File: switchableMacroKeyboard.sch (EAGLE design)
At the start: 33 parts

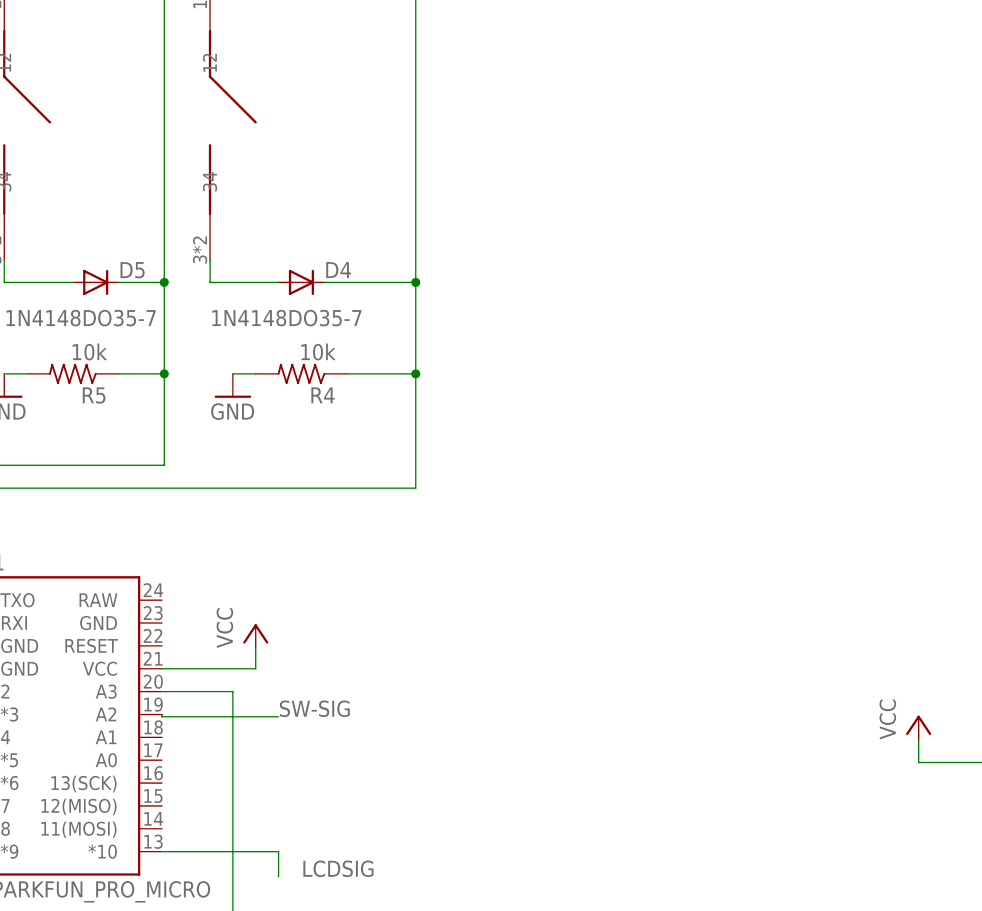
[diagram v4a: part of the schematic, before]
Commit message: Added an enable option to disable all output when broken for debugging purposes. Mitered all of the traces with a 40 mil miter. Changed the corners from filets to chamfers.
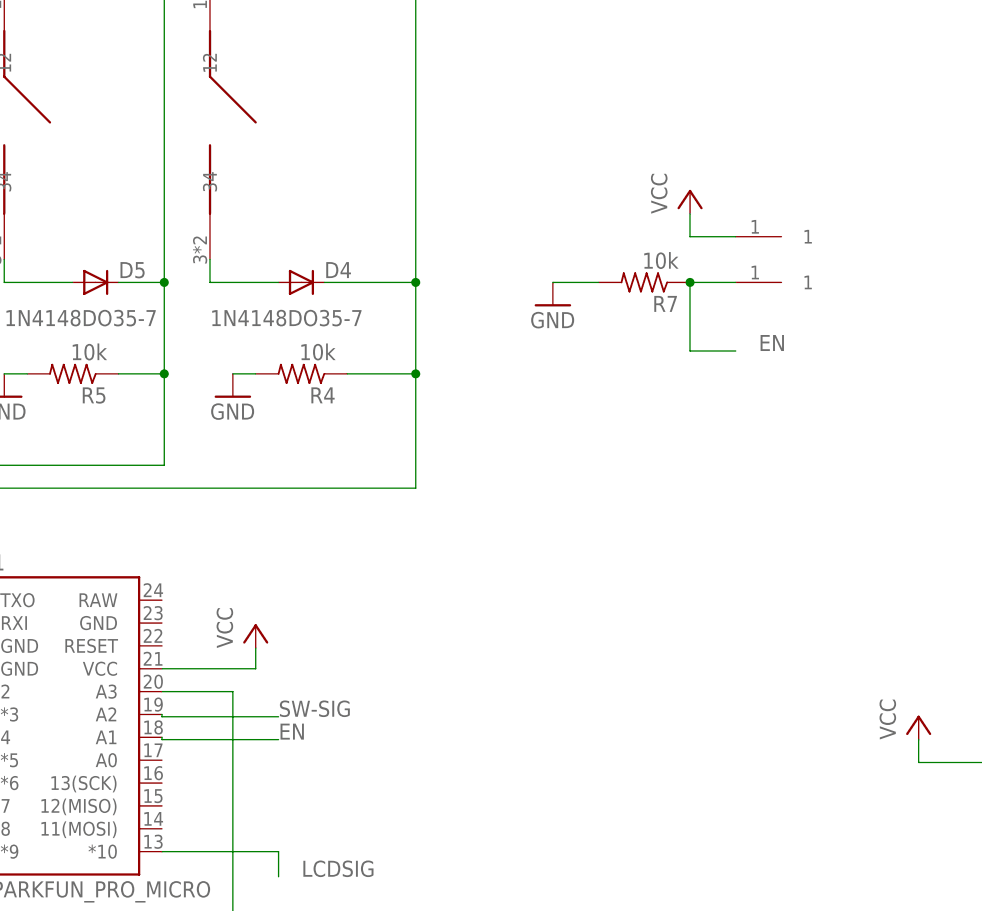
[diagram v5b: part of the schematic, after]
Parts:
- added R7: 10k, rcl:R-US_0207/10
- added U$1, U$2: TESTPOINT, ARNEConnectors:TESTPOINT
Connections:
- new net EN: B1.A1, R7.1, U$2.1
- net GND: now also R7.2
- net VCC: now also U$1.1
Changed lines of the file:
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@@
 <part name="GND6" library="supply1" library_urn="urn:adsk.eagle:library:371" deviceset="GND" device=""/>
 <part name="GND7" library="supply1" library_urn="urn:adsk.eagle:library:371" deviceset="GND" device=""/>
+<part name="U$1" library="ARNEConnectors" deviceset="TESTPOINT" device=""/>
+<part name="U$2" library="ARNEConnectors" deviceset="TESTPOINT" device=""/>
+<part name="R7" library="rcl" library_urn="urn:adsk.eagle:library:334" deviceset="R-US_" device="0207/10" package3d_urn="urn:adsk.eagle:package:23491/2" value="10k"/>
+<part name="GND8" library="supply1" library_urn="urn:adsk.eagle:library:371" deviceset="GND" device=""/>
+<part name="P+5" library="supply1" library_urn="urn:adsk.eagle:library:371" deviceset="VCC" device=""/>
 </parts>
 <sheets>
@@
 <instance part="GND7" gate="1" x="2.54" y="10.16" smashed="yes">
 <attribute name="VALUE" x="0" y="7.62" size="1.778" layer="96"/>
+</instance>
+<instance part="U$1" gate="G$1" x="106.68" y="27.94" smashed="yes"/>
+<instance part="U$2" gate="G$1" x="106.68" y="22.86" smashed="yes"/>
+<instance part="R7" gate="G$1" x="96.52" y="22.86" smashed="yes" rot="R180">
+<attribute name="NAME" x="100.33" y="21.3614" size="1.778" layer="95" rot="R180"/>
+<attribute name="VALUE" x="100.33" y="26.162" size="1.778" layer="96" rot="R180"/>
+</instance>
+<instance part="GND8" gate="1" x="86.36" y="20.32" smashed="yes">
+<attribute name="VALUE" x="83.82" y="17.78" size="1.778" layer="96"/>
+</instance>
+<instance part="P+5" gate="VCC" x="101.6" y="33.02" smashed="yes">
+<attribute name="VALUE" x="99.06" y="30.48" size="1.778" layer="96" rot="R90"/>
 </instance>
 </instances>
@@
 <wire x1="127" y1="-30.48" x2="127" y2="-27.94" width="0.1524" layer="91"/>
 </segment>
+<segment>
+<pinref part="P+5" gate="VCC" pin="VCC"/>
+<pinref part="U$1" gate="G$1" pin="1"/>
+<wire x1="101.6" y1="30.48" x2="101.6" y2="27.94" width="0.1524" layer="91"/>
+<wire x1="101.6" y1="27.94" x2="106.68" y2="27.94" width="0.1524" layer="91"/>
+</segment>
 </net>
 <net name="N$9" class="0">
@@
 <pinref part="GND5" gate="1" pin="GND"/>
 <wire x1="53.34" y1="12.7" x2="50.8" y2="12.7" width="0.1524" layer="91"/>
+</segment>
+<segment>
+<pinref part="R7" gate="G$1" pin="2"/>
+<pinref part="GND8" gate="1" pin="GND"/>
+<wire x1="91.44" y1="22.86" x2="86.36" y2="22.86" width="0.1524" layer="91"/>
 </segment>
 </net>
@@
 </segment>
 </net>
+<net name="EN" class="0">
+<segment>
+<pinref part="B1" gate="G$1" pin="A1"/>
+<wire x1="42.926" y1="-27.686" x2="42.926" y2="-27.94" width="0.1524" layer="91"/>
+<wire x1="42.926" y1="-27.94" x2="55.88" y2="-27.94" width="0.1524" layer="91"/>
+<label x="55.88" y="-27.94" size="1.778" layer="95"/>
+</segment>
+<segment>
+<pinref part="U$2" gate="G$1" pin="1"/>
+<pinref part="R7" gate="G$1" pin="1"/>
+<wire x1="101.6" y1="22.86" x2="106.68" y2="22.86" width="0.1524" layer="91"/>
+<wire x1="101.6" y1="22.86" x2="101.6" y2="15.24" width="0.1524" layer="91"/>
+<junction x="101.6" y="22.86"/>
+<wire x1="101.6" y1="15.24" x2="106.68" y2="15.24" width="0.1524" layer="91"/>
+<label x="109.22" y="15.24" size="1.778" layer="95"/>
+</segment>
+</net>

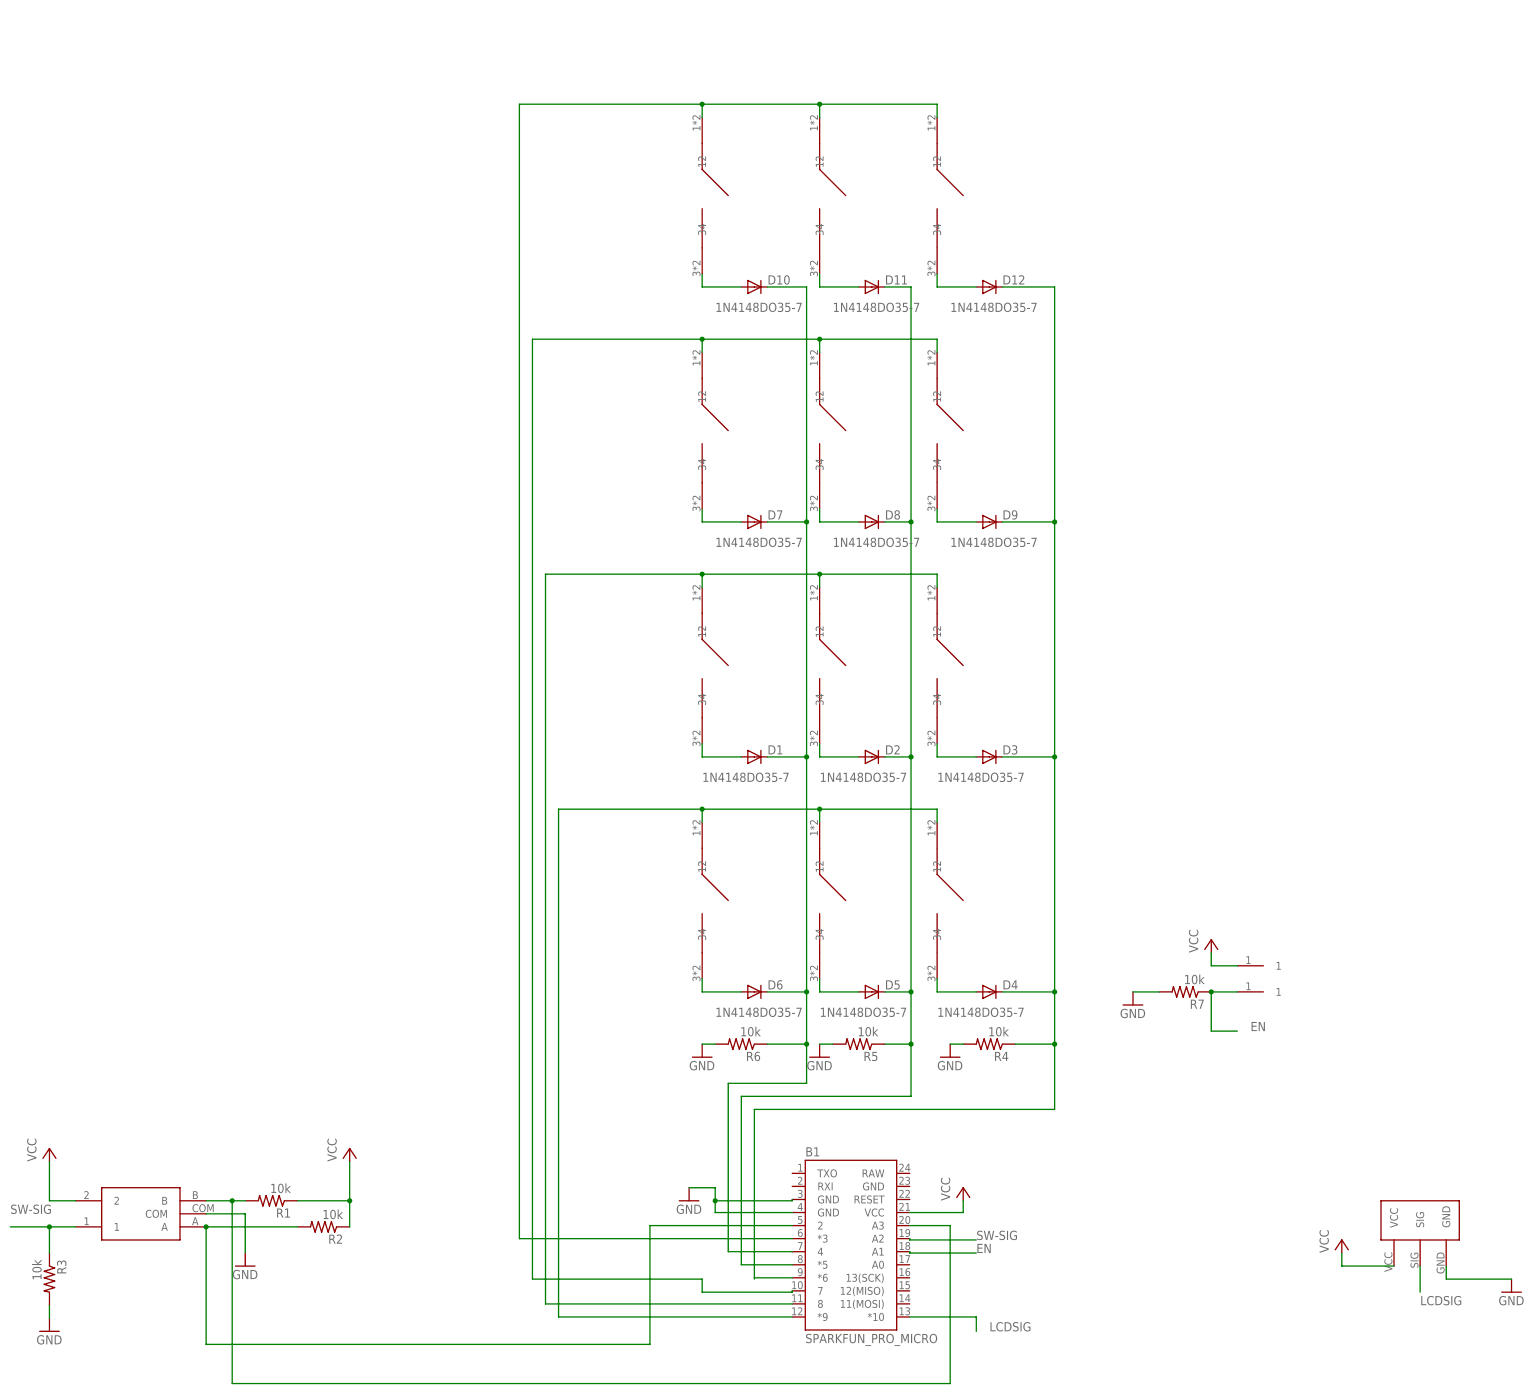
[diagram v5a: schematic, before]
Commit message: Added I2C header for LCD panel. Rearranged pinouts to open up I2C pins on the Pro Micro. To do: add labels to I2C bus and reroute board.
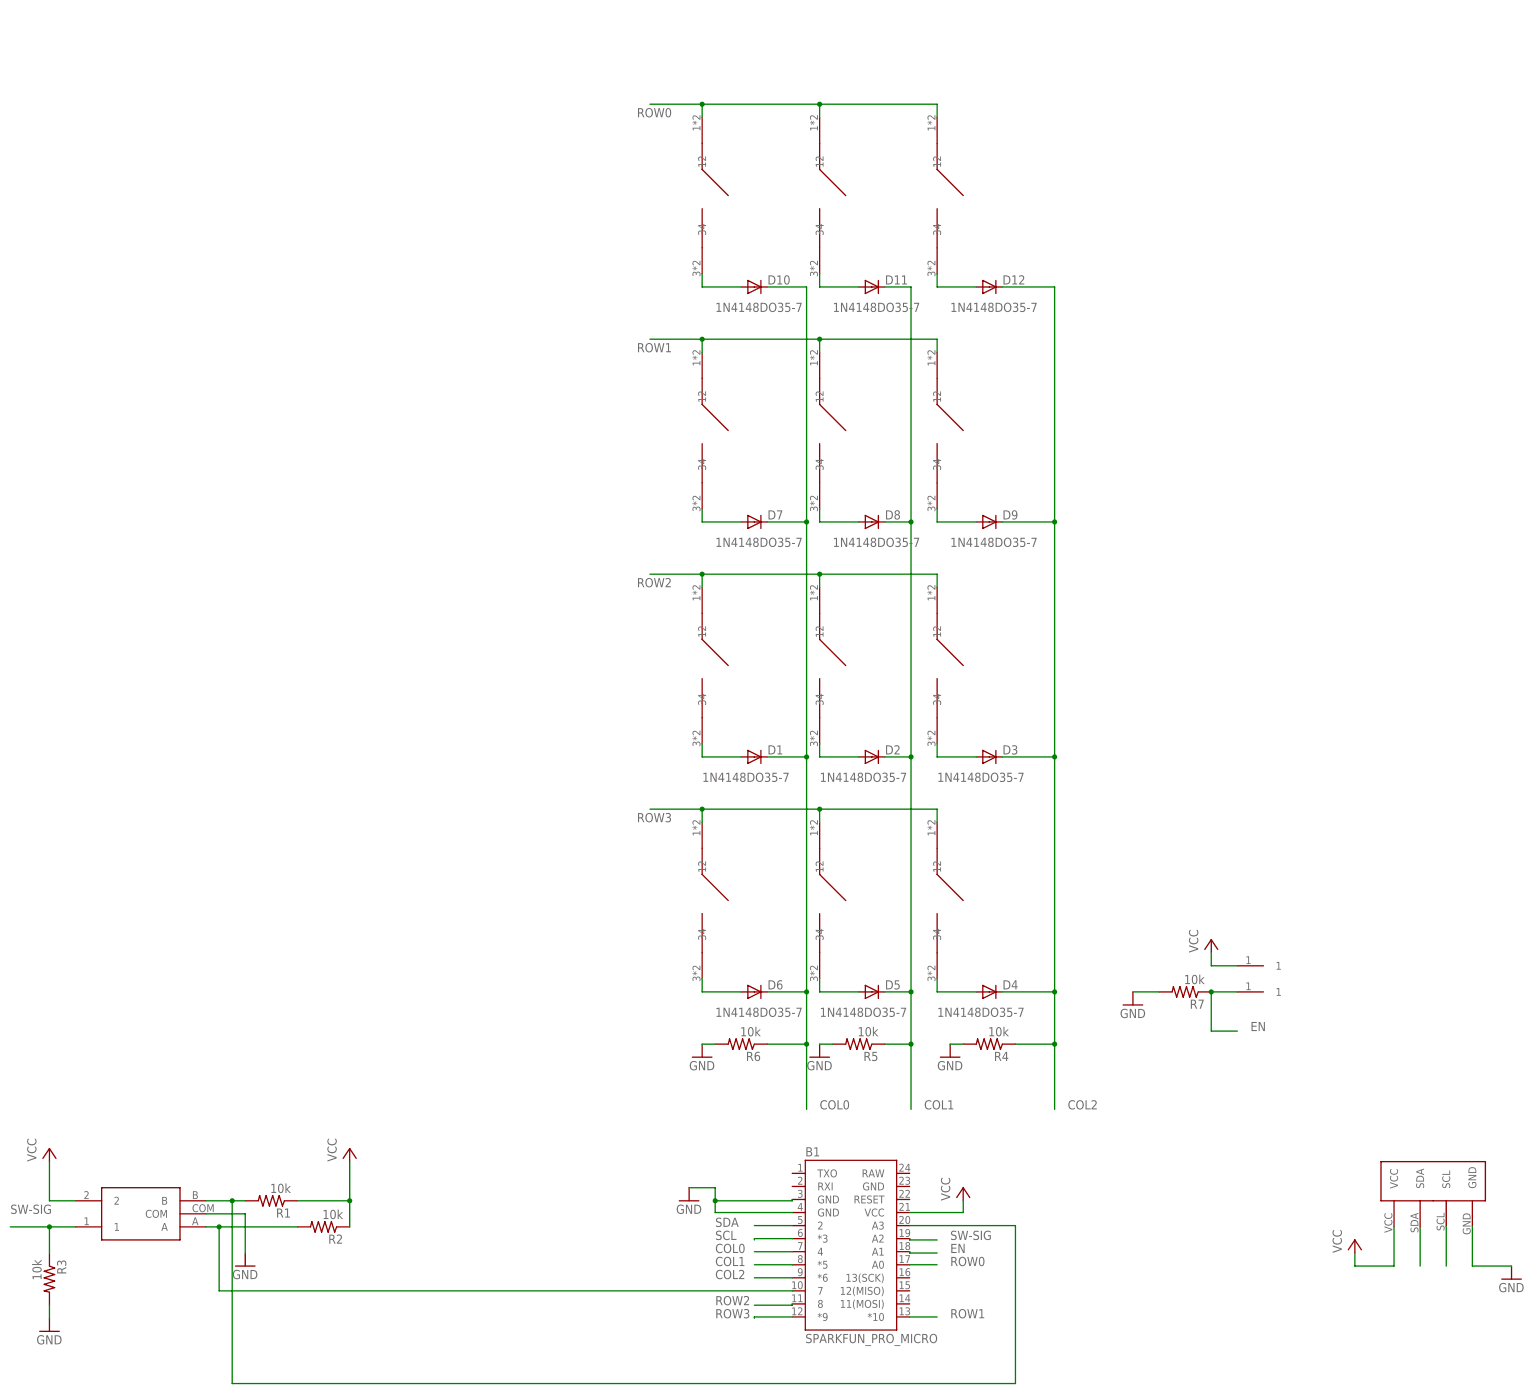
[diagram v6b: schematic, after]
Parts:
- removed U$14: 100MIL3PINSIGNAL, switchableMacroKeyboard:100MIL3PINSIGNAL
- added U$3: I2C-100MIL, ARNEConnectors:I2C-100MIL
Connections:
- net N$10 renamed ROW2
- net N$2 renamed ROW3
- net N$22 renamed COL1
- net N$28 renamed COL0
- net N$30 renamed COL2
- removed net LCDSIG: B1.*10, U$14.SIG
- removed net N$12: B1.2, R2.2, U$13.A
- removed net N$17: 10.12, 11.12, 12.12, B1.7
- removed net N$24: 00.12, 01.12, 02.12, B1.*3
- new net N$1: B1.7, R2.2, U$13.A
- new net ROW0: 00.12, 01.12, 02.12, B1.A0
- new net ROW1: 10.12, 11.12, 12.12, B1.*10
- new net SCL: B1.*3, U$3.SCL
- new net SDA: B1.2, U$3.SDA
- net GND: now also U$3.GND; no longer U$14.GND
- net VCC: now also U$3.VCC; no longer U$14.VCC
